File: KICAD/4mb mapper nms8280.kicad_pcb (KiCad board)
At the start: 2 copper layers, 102.2 x 68.2 mm, 28 parts, among them IC131 74LS125, IC131B1 74LS125, IC131C1 74LS125, IC147 74LS157, IC147B1 74LS157, IC149 74LS670, IC149B1 74LS670, IC157B1 74LS08, IC180B1 74LS00, J1 Conn_01x10_Pin, U1 HY5117404B, U2 HY5117404B

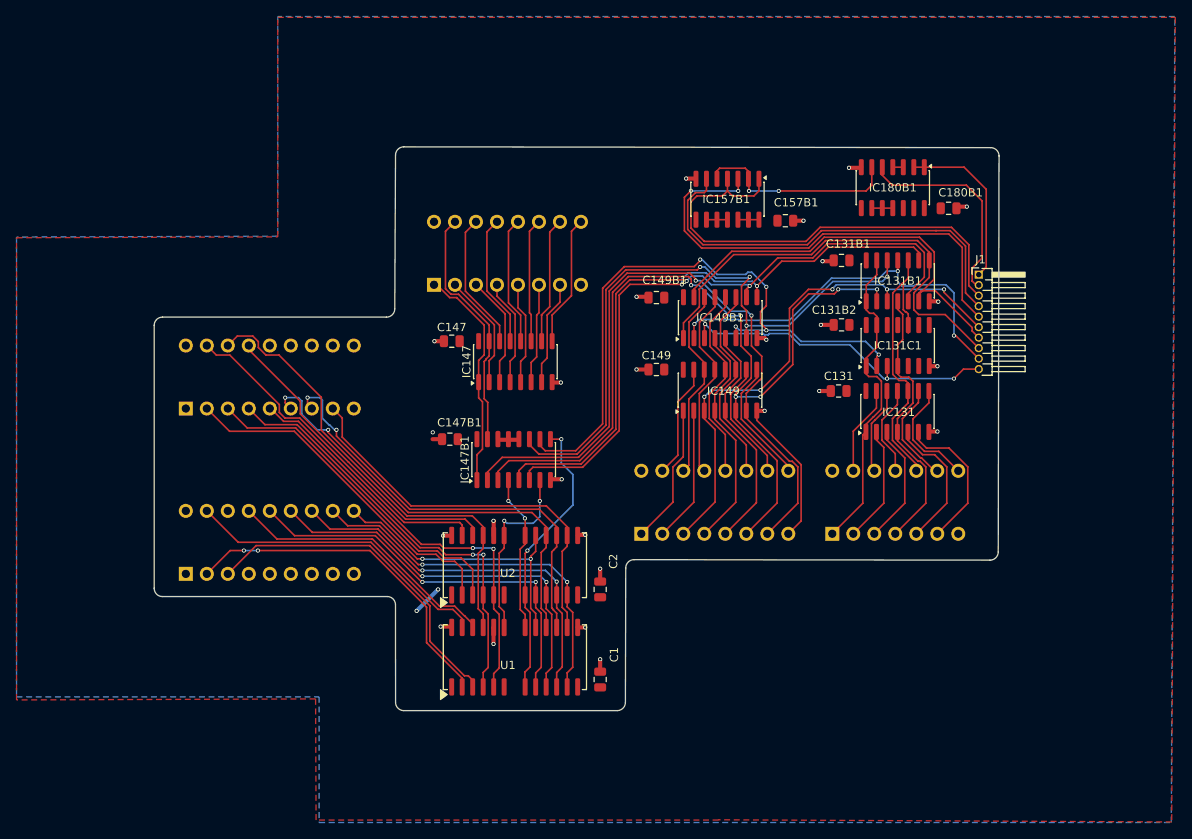
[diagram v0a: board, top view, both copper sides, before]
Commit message: Publish 4 MB mapper project
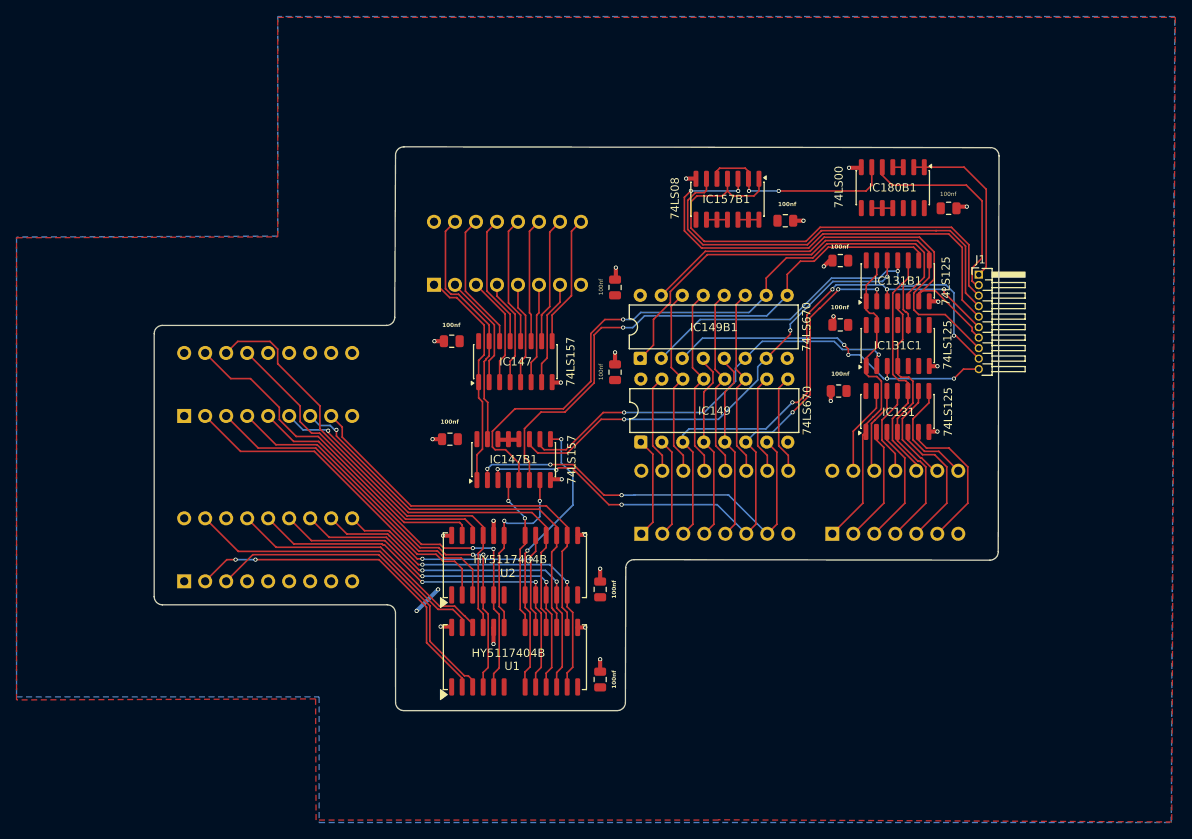
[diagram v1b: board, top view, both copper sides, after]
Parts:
- IC149, IC149B1: footprint Package_SO:SOIC-16_3.9x9.9mm_P1.27mm -> Package_DIP:DIP-16_W7.62mm
- moved IC149 11.5 mm to (156.9, 98.7)
- moved IC149B1 10.9 mm to (156.8, 88.5)
- moved C149B1 5.15 mm to (153.8, 80.0), turned to 90 degrees
- moved C149 5.01 mm to (153.8, 90.2), turned to 90 degrees
- moved CONN133 0.92 mm to (101.7, 87.9)
- moved CONN134 0.92 mm to (101.7, 107.9)
- moved C131B1 0.15 mm to (181.1, 76.7)
- moved C131B2 0.15 mm to (181.1, 84.5)
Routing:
- net /4mb mapper nms8280/IC149_P7: track 87.5 -> 51.1 mm, vias 2 -> 3
- net /4mb mapper nms8280/IC149_P6: track 112.2 -> 78.0 mm
- net Net-(IC131C1-1D): track 77.5 -> 51.2 mm, vias 5 -> 2
- net GND: track 51.8 -> 31.1 mm, vias 26 -> 24
- net Net-(IC131B1-4D): track 77.7 -> 57.6 mm, vias 4 -> 3
- net Net-(IC131B1-3O): track 55.1 -> 61.6 mm
- net /4mb mapper nms8280/IC149_P5_IC149B: track 29.3 -> 23.1 mm
- net Net-(IC131B1-3D): track 74.1 -> 69.4 mm, vias 2 -> 1
- net /4mb mapper nms8280/IC149_P1: track 17.0 -> 12.3 mm
- net /4mb mapper nms8280/IC149_P4_IC149B: track 27.8 -> 23.1 mm
- net /4mb mapper nms8280/IC149_P2: track 16.5 -> 12.1 mm
- net /ram section/A5_IC133/134_P7: track 52.6 -> 48.5 mm, vias 2 -> 1
- net /ram section/A6_IC133/134_P6: track 53.4 -> 49.4 mm, vias 2 -> 1
- net Net-(IC131B1-4O): track 48.6 -> 52.5 mm, vias 3 -> 2
- net /4mb mapper nms8280/IC149_P9: track 15.4 -> 12.0 mm
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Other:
- outline, holes or cut-outs redrawn
- board text added: "J1 - to IC180 pin 12 J2 - to R130 J3 - to IC111 pin 2 J4 - to R127 J5 - to R128 J6 - to IC161 pin 11 J7 - to IC176 pin 11 J8 - to IC176 pin 13 J9 - to IC178 pin 5 J10 - to IC178 pin 7"
